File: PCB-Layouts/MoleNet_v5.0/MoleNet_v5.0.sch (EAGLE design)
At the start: 47 parts, among them J3 693072010801, Q1 MOSFET-NCHANNELBSS138, U1 STM32L073RZT6, U2 SN74LVC1G240DBVR, U3 MCP1703-1802E/DB, X1 8MHz, X2 32kHz, X3 R141426

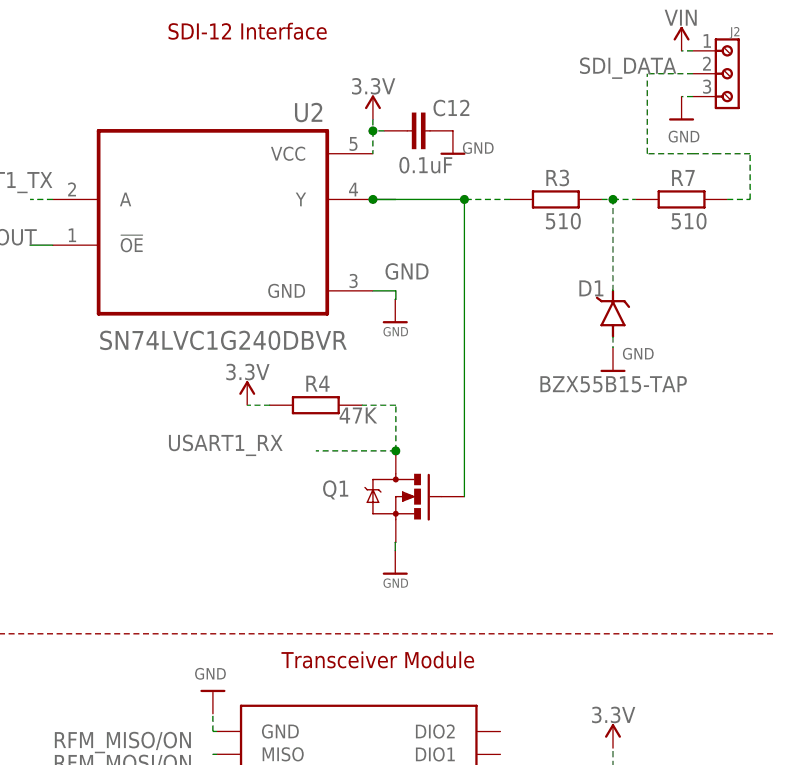
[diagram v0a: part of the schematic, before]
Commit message: Added footprints for the SDI-12 interface components
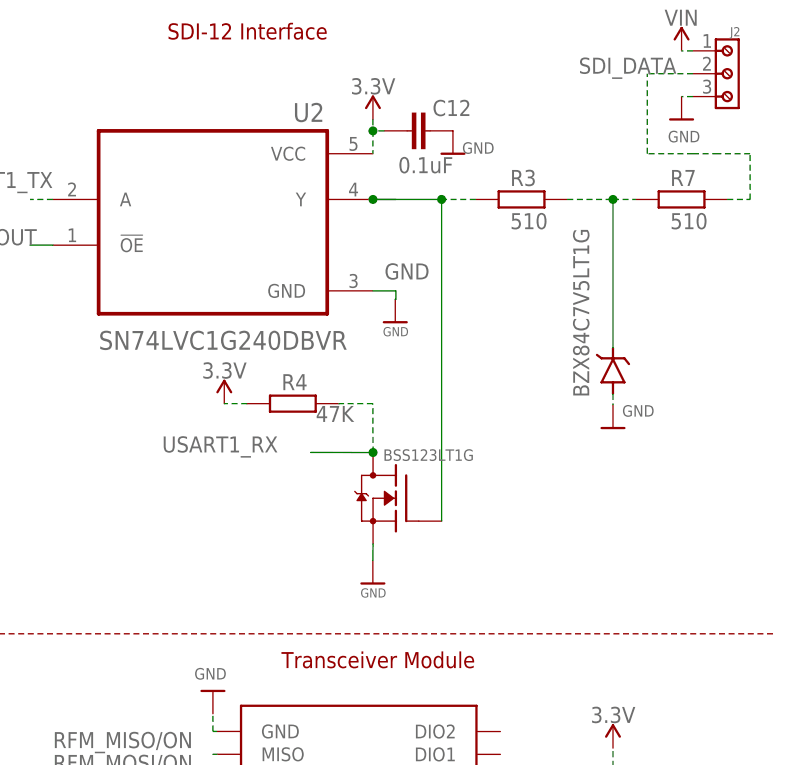
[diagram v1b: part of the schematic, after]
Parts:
- removed D1: BZX55B15-TAP, Diodes-2:BZX55B15-TAP
- removed Q1: MOSFET-NCHANNELBSS138, BeagleBone_Blue_R3:MOSFET-NCHANNELBSS138
- added U$32: BZX84C7V5LT1G_STYLE-8, BZX84C7V5LT1G:BZX84C7V5LT1G_STYLE-8
- added U$33: BSS123LT1G_STYLE-21, BSS123LT1G:BSS123LT1G_STYLE-21
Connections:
- net GND: now also U$32.A, U$33.S; no longer D1.A, Q1.S
- net N$2: now also U$32.C; no longer D1.C
- net N$3: now also U$33.G; no longer Q1.G
- net USART1_RX: now also U$33.D; no longer Q1.D
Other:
- moved on the sheet: R3, R4

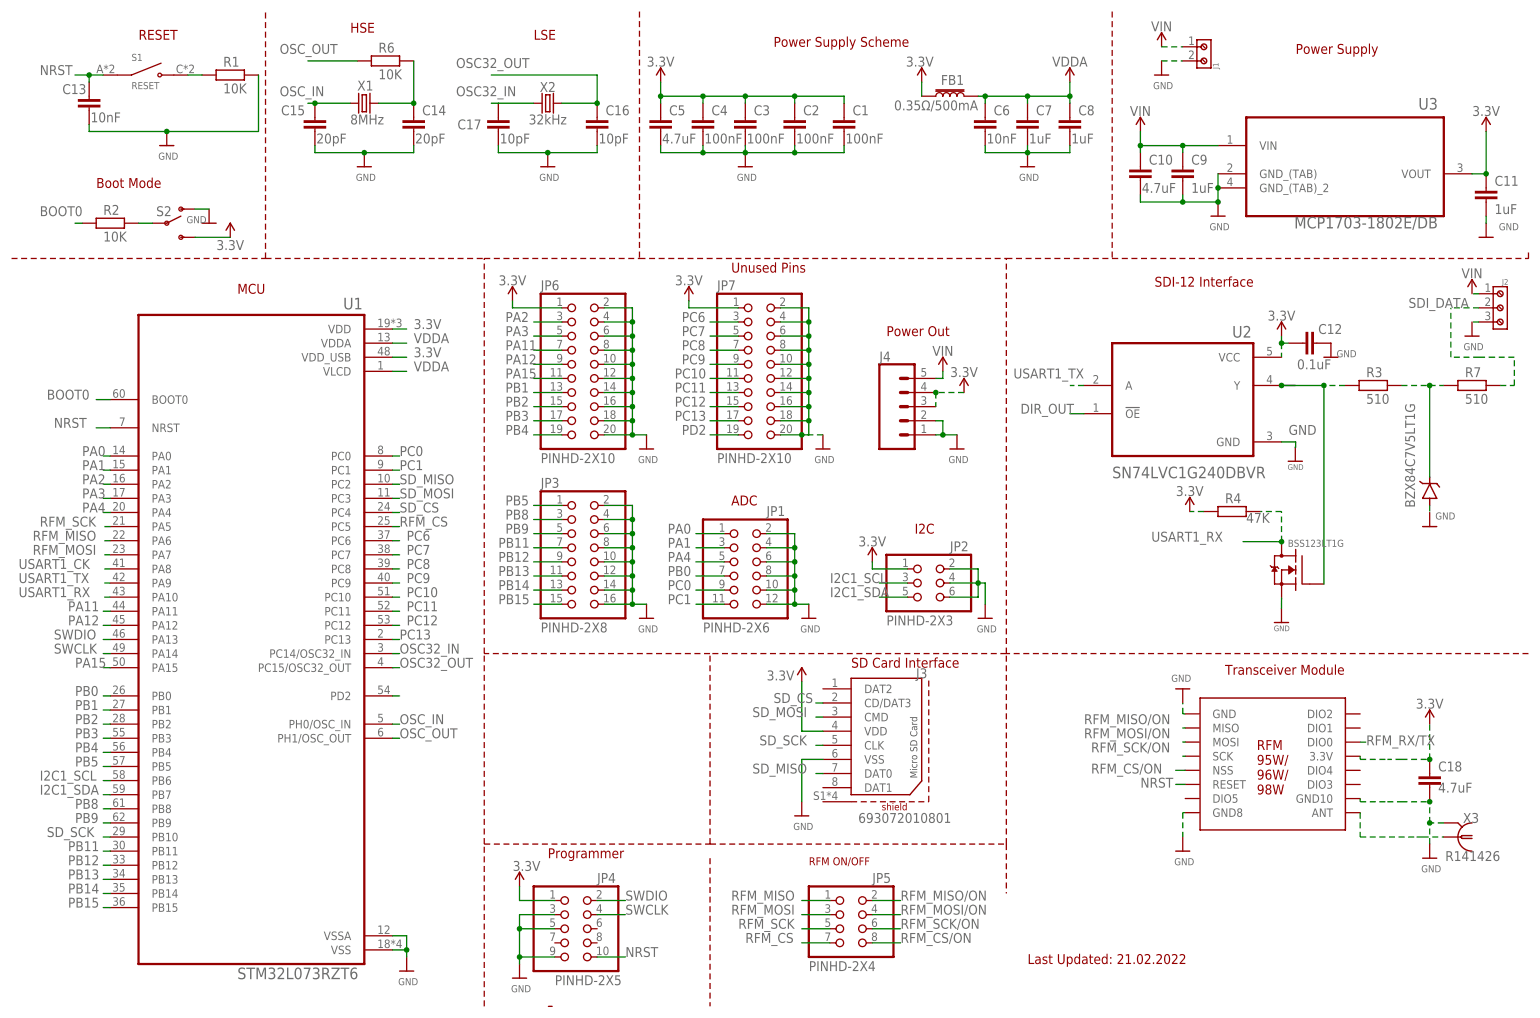
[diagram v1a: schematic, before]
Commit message: componens inconsistency errors fixed, components on PCB arranged
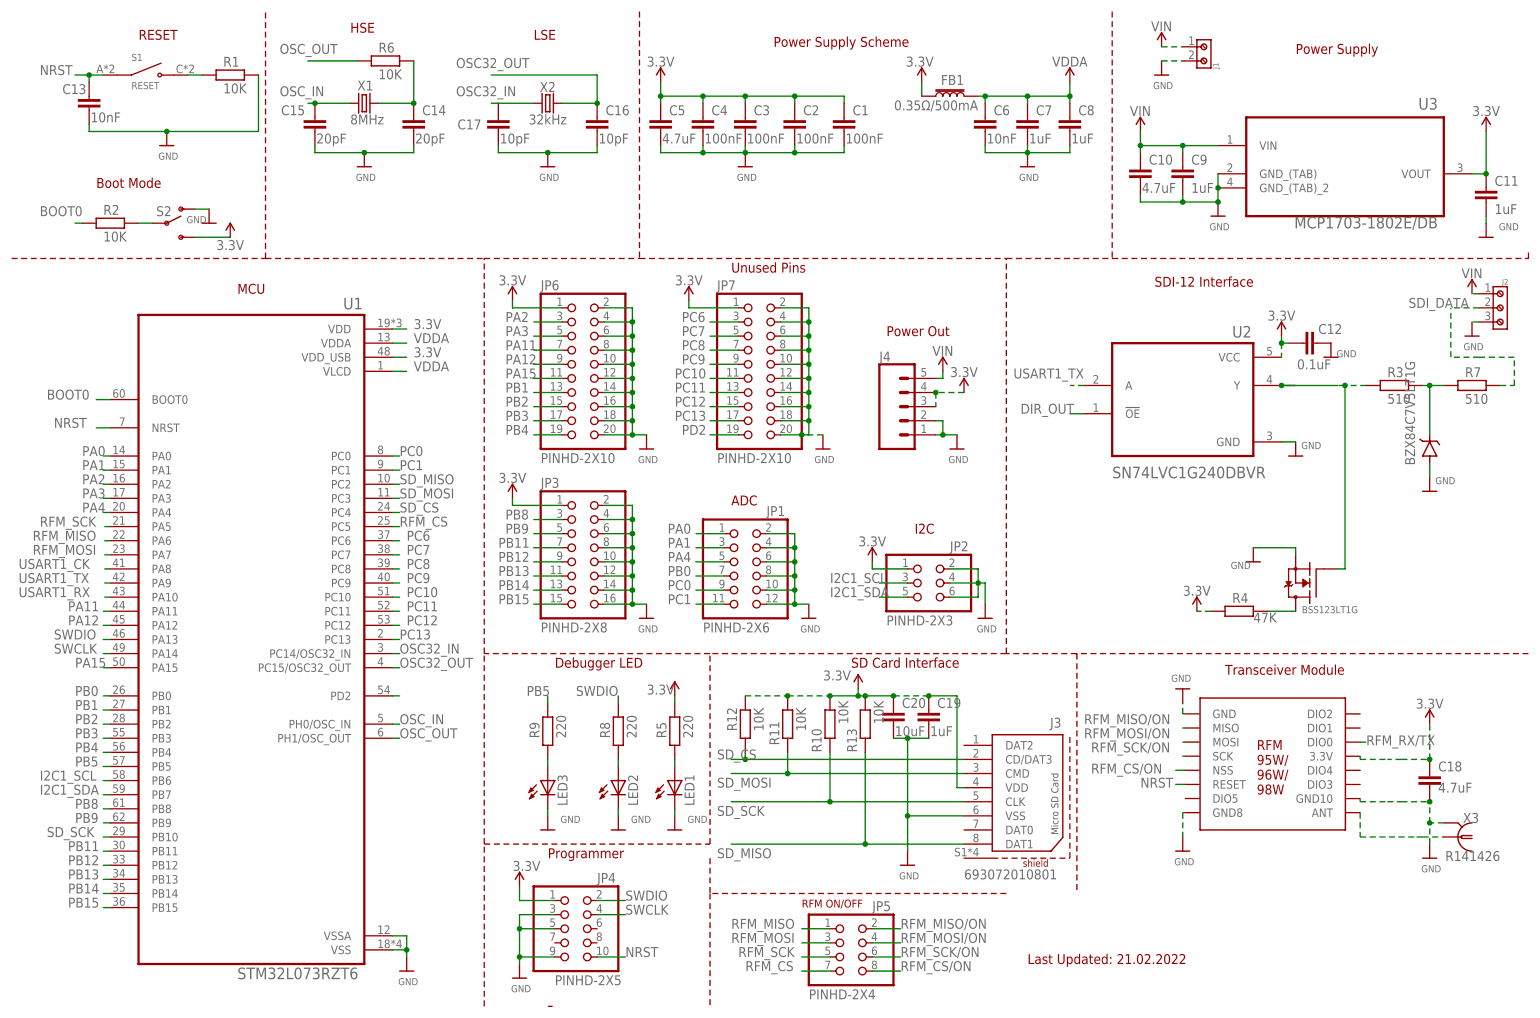
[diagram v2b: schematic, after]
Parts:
- removed U$33: BSS123LT1G_STYLE-21, BSS123LT1G:BSS123LT1G_STYLE-21
- added C19: 1uF, rcl:C-EUC0805
- added C20: 10uF, rcl:C-EUC0805
- added LED1, LED2, LED3: (no value), adafruit:LEDCHIPLED_0805
- added R10, R11, R12, R13: 10K, resistor:R-EU_R0805
- added R5, R8, R9: 220, resistor:R-EU_R0805
- added U$34: BZX84C7V5LT1G_STYLE-8, BZX84C7V5LT1G:BZX84C7V5LT1G_STYLE-8
- U$32: value BZX84C7V5LT1G_STYLE-8 -> BSS123LT1G_STYLE-21; device BZX84C7V5LT1G:BZX84C7V5LT1G_STYLE-8 -> BSS123LT1G:BSS123LT1G_STYLE-21
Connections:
- new net N$11: R4.2, U$32.D
- new net N$7: LED1.A, R5.1
- new net N$8: LED2.A, R8.1
- new net N$9: LED3.A, R9.1
- net 3.3V: now also C19.1, C20.1, JP3.1, R10.2, R11.2, R12.2, R13.2, R5.2
- net GND: now also C19.2, C20.2, LED1.C, LED2.C, LED3.C, U$32.S, U$34.A; no longer U$32.A, U$33.S
- net N$2: now also U$34.C; no longer U$32.C
- net N$3: now also U$32.G; no longer U$33.G
- net PB5: now also R9.2; no longer JP3.1
- net SD_CS: now also R12.1
- net SD_MISO: now also J3.DAT1, R13.1; no longer J3.DAT0
- net SD_MOSI: now also R11.1
- net SD_SCK: now also R10.1
- net SWDIO: now also R8.2
- net USART1_RX: no longer R4.2, U$33.D
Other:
- note added: "Debugger LED"
- moved on the sheet: J3, JP5, R3, R4

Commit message: ERC errors and warnings are fixed
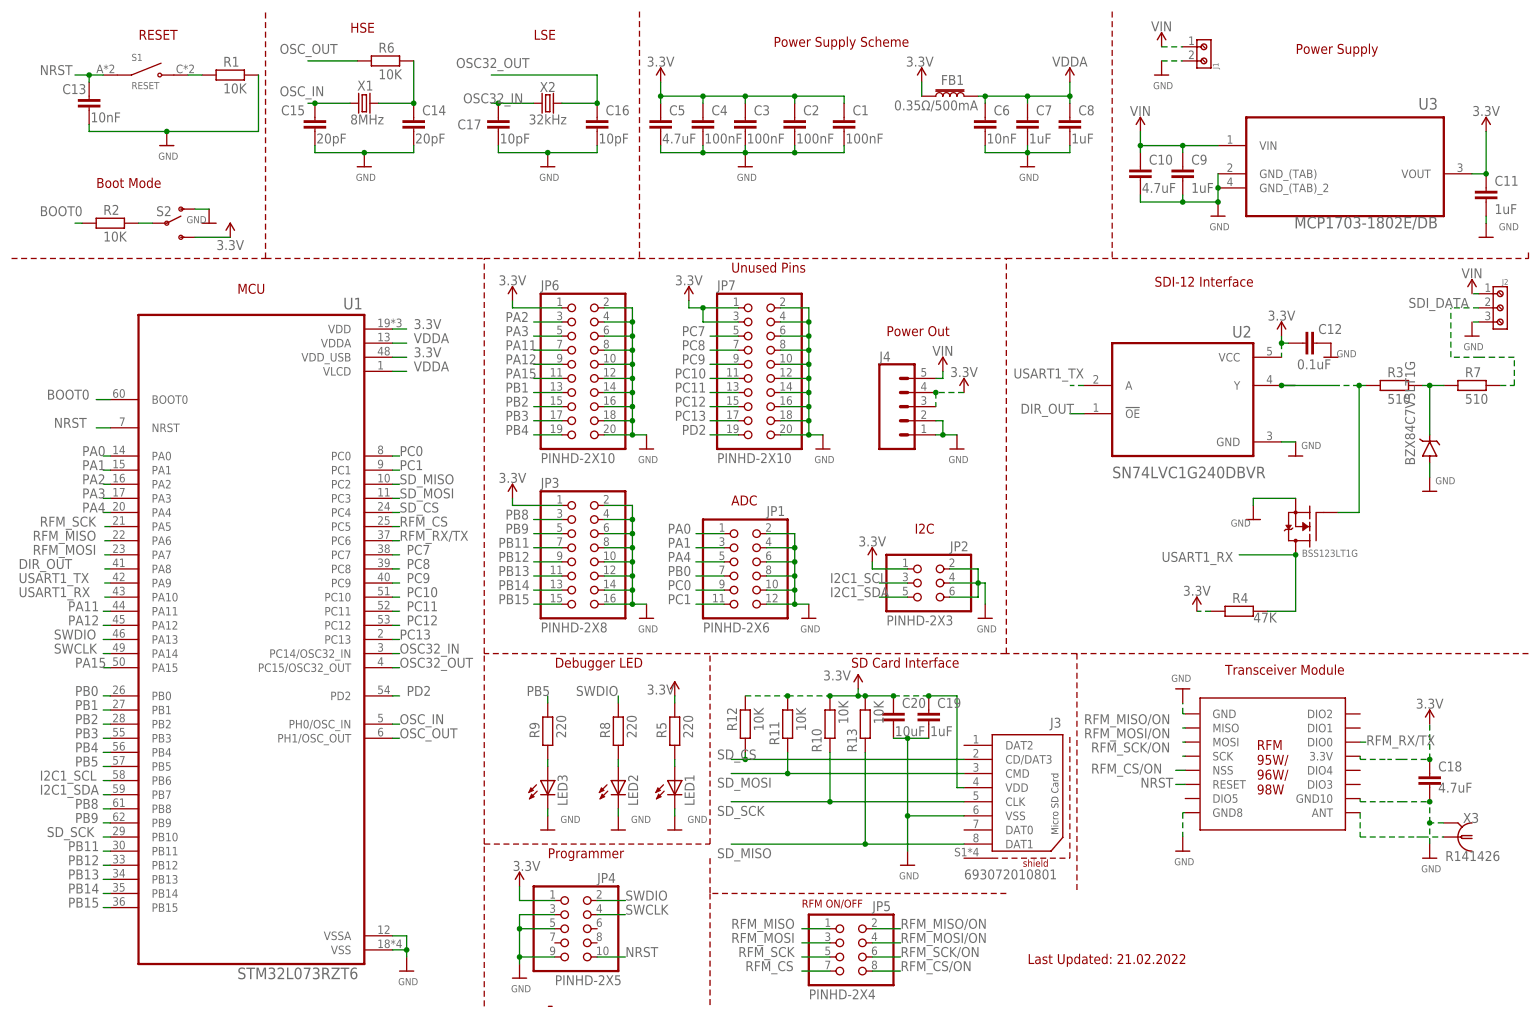
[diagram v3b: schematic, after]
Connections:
- removed net N$11: R4.2, U$32.D
- removed net N$19: U1.PD2
- removed net PC6: JP7.3, U1.PC6
- removed net USART1_CK: U1.PA8
- net 3.3V: now also JP7.3
- net DIR_OUT: now also U1.PA8
- net PD2: now also U1.PD2
- net RFM_RX/TX: now also U1.PC6
- net USART1_RX: now also R4.2, U$32.D
